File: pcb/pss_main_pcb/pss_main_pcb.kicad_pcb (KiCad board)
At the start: 2 copper layers, 177.8 x 55.9 mm, 97 parts, among them J1 24V DC Input, J2 220V AC Input, J3 Hot Air Gun, J4 Soldering Iron, J5 STM32_Prog, J6 UART_Prog, Q1 BC817, Q2 MMBT2222, Q3 MMBT2907, Q4 IRLML9301T, Q5 IRFZ44S, Q6 BT139B-800, SW1 Hot Air Gun Input, SW2 Soldering Iron Input, SW3 SW_Push, SW4 Main Encoder Input, SW5 EN, SW6 Boot, U1 LM2596S-5, U2 LM2596S-3.3, U3 MOC3023S, U4 LM358, U5 STM32F030K6Tx, U6 ESP32-WROOM-32U, U7 2.8inch_SPI_Module_ILI9341_SK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

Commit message: Change footprints
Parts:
- removed the C1 at (190.5, 138.4)
- removed the C7 at (94.0, 130.8)
- removed the C9 at (135.9, 138.4)
- added C4: 1uF 50V, Capacitor_SMD:CP_Elec_4x5.4, F.Cu at (109.2, 163.8)
- added C8: 10u 16V, Capacitor_SMD:CP_Elec_4x5.4, F.Cu at (130.8, 132.1)
- C5: value 1uF 50V -> 0.1u Y; footprint Capacitor_SMD:CP_Elec_16x17.5 -> Capacitor_THT:C_Rect_L10.0mm_W2.5mm_P7.50mm_MKS4
- C6: value 0.1u Y -> 47u 50V; footprint Capacitor_THT:C_Rect_L10.0mm_W2.5mm_P7.50mm_MKS4 -> Capacitor_SMD:CP_Elec_8x10.5
- L1, L2: footprint Inductor_SMD:L_12x12mm_H8mm -> Inductor_SMD:L_Taiyo-Yuden_NR-30xx_HandSoldering
- L3: footprint Inductor_SMD:L_Wuerth_HCI-1030 -> Inductor_SMD:L_Taiyo-Yuden_NR-30xx_HandSoldering
- Q5: footprint Package_TO_SOT_THT:TO-220-3_Vertical -> Package_TO_SOT_SMD:TO-263-2
- moved D2 316.4 mm to (180.3, 151.1)
- moved D1 312.6 mm to (180.3, 142.2)
- moved J5 308.9 mm to (113.0, 80.0), turned to 270 degrees
- moved D8 308.5 mm to (115.6, 125.7)
- moved D7 286.1 mm to (133.3, 124.5)
- moved D6 279.3 mm to (125.7, 125.7)
- moved D3 259.0 mm to (305.0, 165.1)
- moved C3 252.6 mm to (223.5, 137.2)
- moved C2 245.6 mm to (238.8, 137.2)
- moved SW3 242.5 mm to (163.8, 69.8)
- moved Q1 229.5 mm to (96.5, 168.9)
- moved C6 220.1 mm to (92.7, 161.2), turned to 270 degrees
- moved Q5 195.0 mm to (108.0, 144.8), turned to 270 degrees
- moved L2 155.1 mm to (316.2, 148.6)
- moved SW5 144.5 mm to (176.5, 69.8)
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- renumbered C2 to C1, C11 to C10, C12 to C11, C13 to C12, C14 to C13, C15 to C14, C16 to C15, C17 to C16, C18 to C17, C19 to C18, C20 to C19, C3 to C2, C21 to C20, C22 to C21, C4 to C3, C8 to C7, C10 to C9
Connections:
- C5 pad 2: GND -> 220_AC1
- C6 pad 1: Net-(C6-Pad1) -> Hot_Air_Fan
- C6 pad 2: 220_AC1 -> GND
- L3 pad 1: Net-(C5-Pad1) -> Net-(C4-Pad1)
- Q4 pad 3: Net-(C5-Pad1) -> Net-(C4-Pad1)
- R10 pad 2: Net-(C6-Pad1) -> Net-(C5-Pad1)

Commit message: Change footprints and place some new components
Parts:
- C1: value 470u 50V -> 470u 35V; footprint Capacitor_SMD:CP_Elec_16x17.5 -> Capacitor_SMD:CP_Elec_10x10.5
- D6, D7, D8: moved to B.Cu
- J1: footprint Connector_AMASS:AMASS_XT60-F_1x02_P7.20mm_Vertical -> Connector_AMASS:AMASS_XT30U-F_1x02_P5.0mm_Vertical
- J2: footprint Connector:Banana_Jack_3Pin -> Connector_Wire:SolderWire-2.5sqmm_1x03_P7.2mm_D2.4mm_OD3.6mm
- moved R1 286.1 mm to (147.3, 82.5), turned to 270 degrees
- moved D5 237.6 mm to (101.6, 99.1), turned to 90 degrees
- moved R5 237.1 mm to (111.5, 83.8), turned to 180 degrees
- moved R9 232.5 mm to (116.8, 85.3), turned to 270 degrees
- moved Q3 230.0 mm to (111.4, 88.9), turned to 270 degrees
- moved Q2 220.1 mm to (115.9, 91.7), turned to 270 degrees
- moved D3 200.9 mm to (120.7, 85.3), turned to 270 degrees
- moved R19 134.6 mm to (147.3, 76.2), turned to 270 degrees
- moved C12 128.9 mm to (149.9, 76.4), turned to 270 degrees
- moved R11 114.6 mm to (125.5, 83.8)
- moved R18 112.1 mm to (132.1, 88.9), turned to 90 degrees
- moved C7 108.8 mm to (138.4, 82.3), turned to 90 degrees
- moved R17 105.8 mm to (144.8, 76.0), turned to 90 degrees
- moved R12 103.7 mm to (116.8, 80.0), turned to 90 degrees
- moved R20 102.0 mm to (135.9, 87.6), turned to 180 degrees
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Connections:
- J2 pad 1: 220_AC1 -> GNDPWR
- J2 pad 2: GNDPWR -> 220V_Heater2
- J2 pad 3: 220V_Heater2 -> 220_AC1
- J3 pad 4: GNDPWR -> GND
- J3 pad 5: GND -> GNDPWR
- J3 pad 6: Hot_Air_Therm_Pos -> 220V_Heater2
- J3 pad 8: 220V_Heater2 -> Hot_Air_Therm_Pos
- J4 pad 1: Iron_Heat_Neg -> Iron_Heat_Pos
- J4 pad 2: Iron_Heat_Pos -> Iron_Heat_Neg

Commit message: Finish preliminary placement for components
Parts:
- C19, C20, D1, D2, L1, L2, R1, R31, R33, U1, U2: moved to B.Cu
- moved R21 345.4 mm to (81.3, 69.8), turned to 90 degrees
- moved R23 343.9 mm to (88.9, 69.8), turned to 90 degrees
- moved R30 330.4 mm to (84.9, 94.0), turned to 180 degrees
- moved R22 325.0 mm to (106.7, 69.8), turned to 90 degrees
- moved R24 318.3 mm to (114.3, 70.1), turned to 90 degrees
- moved R29 287.0 mm to (110.5, 100.3), turned to 180 degrees
- moved JP1 271.9 mm to (157.5, 88.9)
- moved R27 265.4 mm to (157.5, 69.8), turned to 270 degrees
- moved R25 260.7 mm to (157.3, 86.4)
- moved C17 254.4 mm to (162.6, 95.2), turned to 180 degrees
- moved R28 253.6 mm to (134.6, 94.0)
- moved R26 252.8 mm to (158.8, 93.8), turned to 90 degrees
- moved C18 251.4 mm to (175.3, 77.5)
- moved C14 250.0 mm to (175.3, 80.0)
- moved C15 242.9 mm to (162.6, 92.7), turned to 180 degrees
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
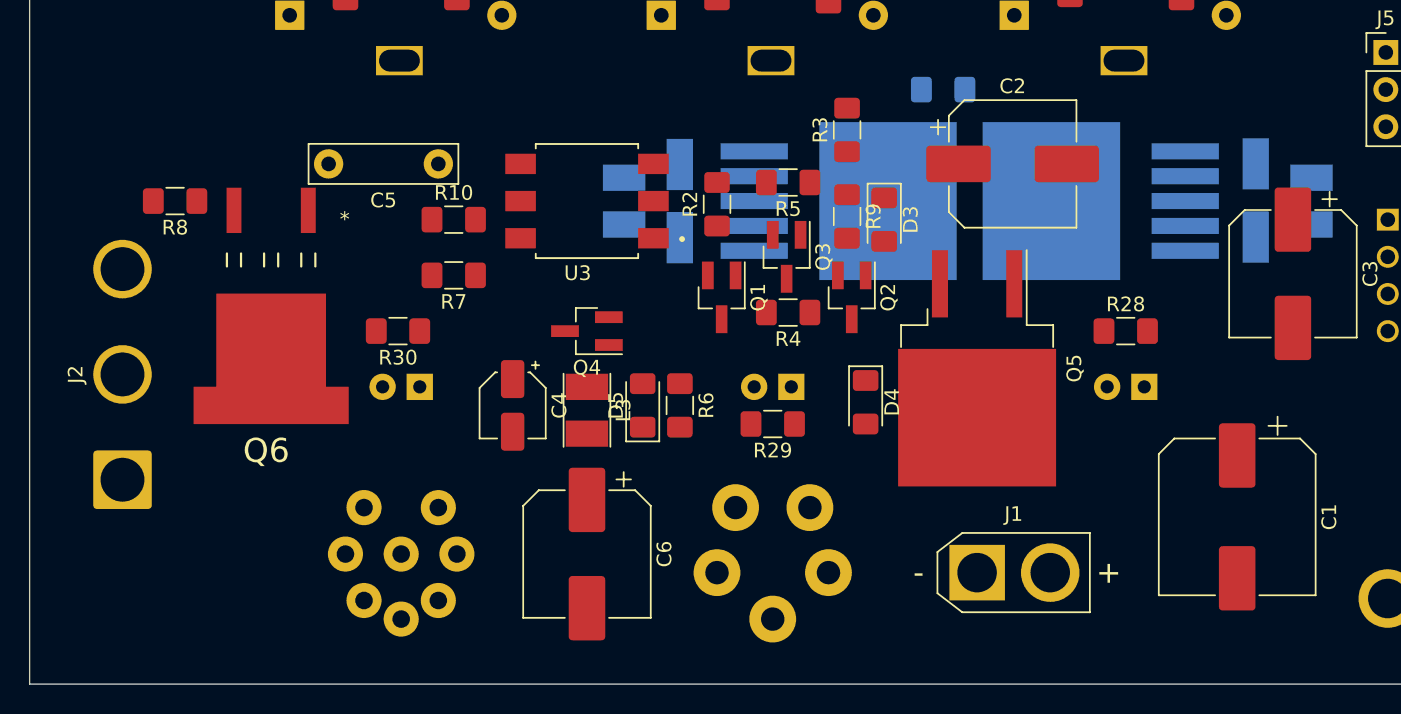
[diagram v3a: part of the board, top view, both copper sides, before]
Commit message: Started pcb routing
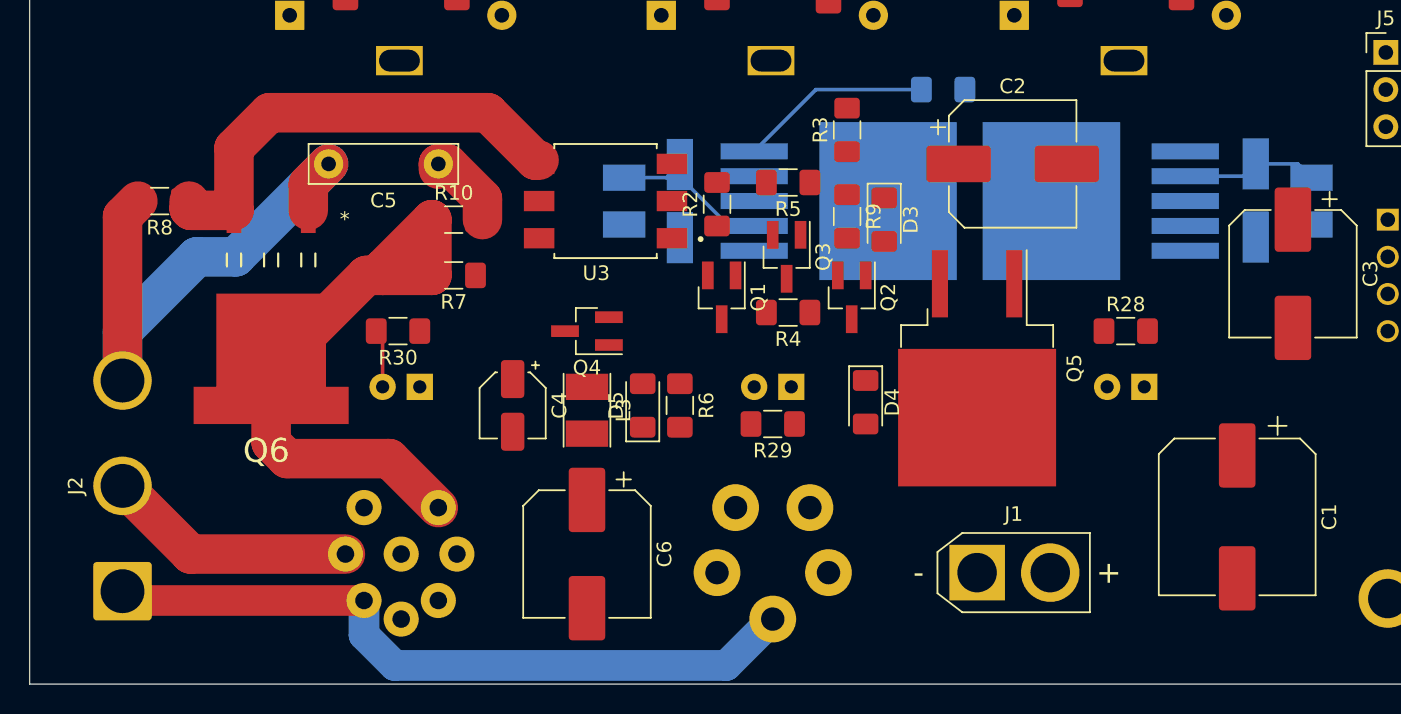
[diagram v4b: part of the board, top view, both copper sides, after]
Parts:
- moved J2 7.62 mm to (66.0, 111.8)
- moved U3 1.27 mm to (99.1, 85.1)
- moved R8 1.05 mm to (68.6, 85.1)
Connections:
- J3 pad 1: Hot_Air_Fan -> 220V_Heater1
- J3 pad 7: 220V_Heater1 -> Hot_Air_Fan
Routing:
- net GNDPWR: track 0.00 -> 49.2 mm
- net 220V_Heater1: track 0.00 -> 42.1 mm
- net 220_AC1: track 0.00 -> 39.4 mm
- net Net-(Q6-Pad3): track 0.00 -> 31.1 mm
- net 220V_Heater2: track 0.00 -> 17.2 mm
- net Enable_5V: track 0.00 -> 13.2 mm
- net Net-(D1-Pad1): track 0.00 -> 11.5 mm
- net Net-(D2-Pad1): track 0.00 -> 9.37 mm
- net Net-(C5-Pad1): track 0.00 -> 5.79 mm
- net Net-(D8-Pad2): track 0.00 -> 3.99 mm
- net +5V: track 0.00 -> 1.74 mm
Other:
- net class Power_220 added: clearance 0.75, trace_width 2.7, via_dia 0.8, via_drill 0.4
- net class Pwr_GND added: clearance 0.2, trace_width 2.1, via_dia 0.8, via_drill 0.4
